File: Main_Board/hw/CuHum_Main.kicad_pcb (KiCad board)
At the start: 2 copper layers, 50 parts, among them J1 Barrel_Jack_Switch_Pin3Ring, J101 Conn_01x07, J102 Conn_01x07, J103 Conn_01x07, J104 Conn_01x07, J105 Conn_01x07, J106 Conn_01x07, J107 Conn_01x07, J108 Conn_01x07, J109 Conn_01x07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

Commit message: (WIP) Main board layout & routing
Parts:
- J101, J102, J103, J104, J105, J106, J107, J108, J109, J110, J111, J112, J113, J114, J115: footprint Connector_PinHeader_2.54mm:PinHeader_1x07_P2.54mm_Vertical -> CuHum_Main_footprints:Unit_1x07_P2.54
- moved J103 103.3 mm to (159.8, 157.2), turned to 38.571 degrees
- moved J104 92.8 mm to (178.0, 119.5), turned to 90 degrees
- moved J102 90.9 mm to (119.2, 166.6), turned to -12.857 degrees
- moved J109 79.0 mm to (138.8, 158.6), turned to 12.8573 degrees
- moved J1 75.5 mm to (145.6, 118.3), turned to 180 degrees
- moved J110 70.4 mm to (166.0, 136.8), turned to 64.2853 degrees
- moved J108 68.3 mm to (104.9, 150.9), turned to -38.5707 degrees
- moved J115 67.2 mm to (100.1, 134.0), turned to 115.714 degrees
- moved C1 65.4 mm to (139.8, 125.7), turned to -90 degrees
- moved J105 62.6 mm to (159.9, 81.8), turned to 141.428 degrees
- moved J114 61.4 mm to (89.9, 119.5), turned to -90 degrees
- moved U1 59.5 mm to (137.1, 124.8), turned to 0 degrees
- moved J101 58.8 mm to (87.8, 141.1), turned to -64.285 degrees
- moved R1 56.3 mm to (134.5, 128.2), turned to 90 degrees
- moved L1 53.6 mm to (134.4, 115.8), turned to 180 degrees
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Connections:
- U5 pad 10: UNIT_CAP_03 -> UNIT_CAP_02
- U5 pad 11: UNIT_CAP_04 -> UNIT_CAP_09
- U5 pad 12: UNIT_CAP_05 -> unconnected-(U5-LED0/ELE4-Pad12)
- U5 pad 13: UNIT_CAP_06 -> UNIT_CAP_03
- U5 pad 14: UNIT_CAP_07 -> unconnected-(U5-LED2/ELE6-Pad14)
- U5 pad 15: UNIT_CAP_08 -> unconnected-(U5-LED3/ELE7-Pad15)
- U5 pad 16: UNIT_CAP_09 -> UNIT_CAP_10
- U5 pad 17: UNIT_CAP_10 -> unconnected-(U5-LED5/ELE9-Pad17)
- U5 pad 18: UNIT_CAP_11 -> UNIT_CAP_04
- U5 pad 19: UNIT_CAP_12 -> UNIT_CAP_11
- U5 pad 8: UNIT_CAP_01 -> UNIT_CAP_15
- U5 pad 9: UNIT_CAP_02 -> UNIT_CAP_08
- U6 pad 10: UNIT_CAP_15 -> UNIT_CAP_12
- U6 pad 13: unconnected-(U6-LED1/ELE5-Pad13) -> UNIT_CAP_06
- U6 pad 15: unconnected-(U6-LED3/ELE7-Pad15) -> UNIT_CAP_13
- U6 pad 17: unconnected-(U6-LED5/ELE9-Pad17) -> UNIT_CAP_07
- U6 pad 18: unconnected-(U6-LED6/ELE10-Pad18) -> UNIT_CAP_14
- U6 pad 19: unconnected-(U6-LED7/ELE11-Pad19) -> UNIT_CAP_01
- U6 pad 8: UNIT_CAP_13 -> unconnected-(U6-ELE0-Pad8)
- U6 pad 9: UNIT_CAP_14 -> UNIT_CAP_05
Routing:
- net SPI2_MOSI: track 0.00 -> 368.9 mm, vias 0 -> 13
- net SPI2_SCK: track 0.00 -> 356.1 mm, vias 0 -> 13
- net VDD: track 8.27 -> 85.3 mm, vias 4 -> 6
- net I2C1_SDA: track 0.00 -> 70.1 mm, vias 0 -> 3
- net I2C1_SCL: track 0.00 -> 67.7 mm, vias 0 -> 2
- net UNIT_CAP_01: track 0.00 -> 59.7 mm
- net UNIT_CAP_04: track 0.00 -> 53.3 mm
- net UNIT_CAP_11: track 0.00 -> 51.8 mm
- net UNIT_CAP_14: track 0.00 -> 44.1 mm
- net UNIT_CAP_07: track 0.00 -> 41.3 mm
- net UNIT_CAP_05: track 0.00 -> 39.5 mm
- net GND: track 11.4 -> 43.0 mm, vias 25 -> 46
- net UNIT_CAP_10: track 0.00 -> 31.5 mm
- net UNIT_CAP_03: track 0.00 -> 31.4 mm
- net UNIT_CAP_08: track 0.00 -> 30.7 mm
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- added copper zone on B.Cu, net GND
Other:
- board outline added: 100 x 100 mm

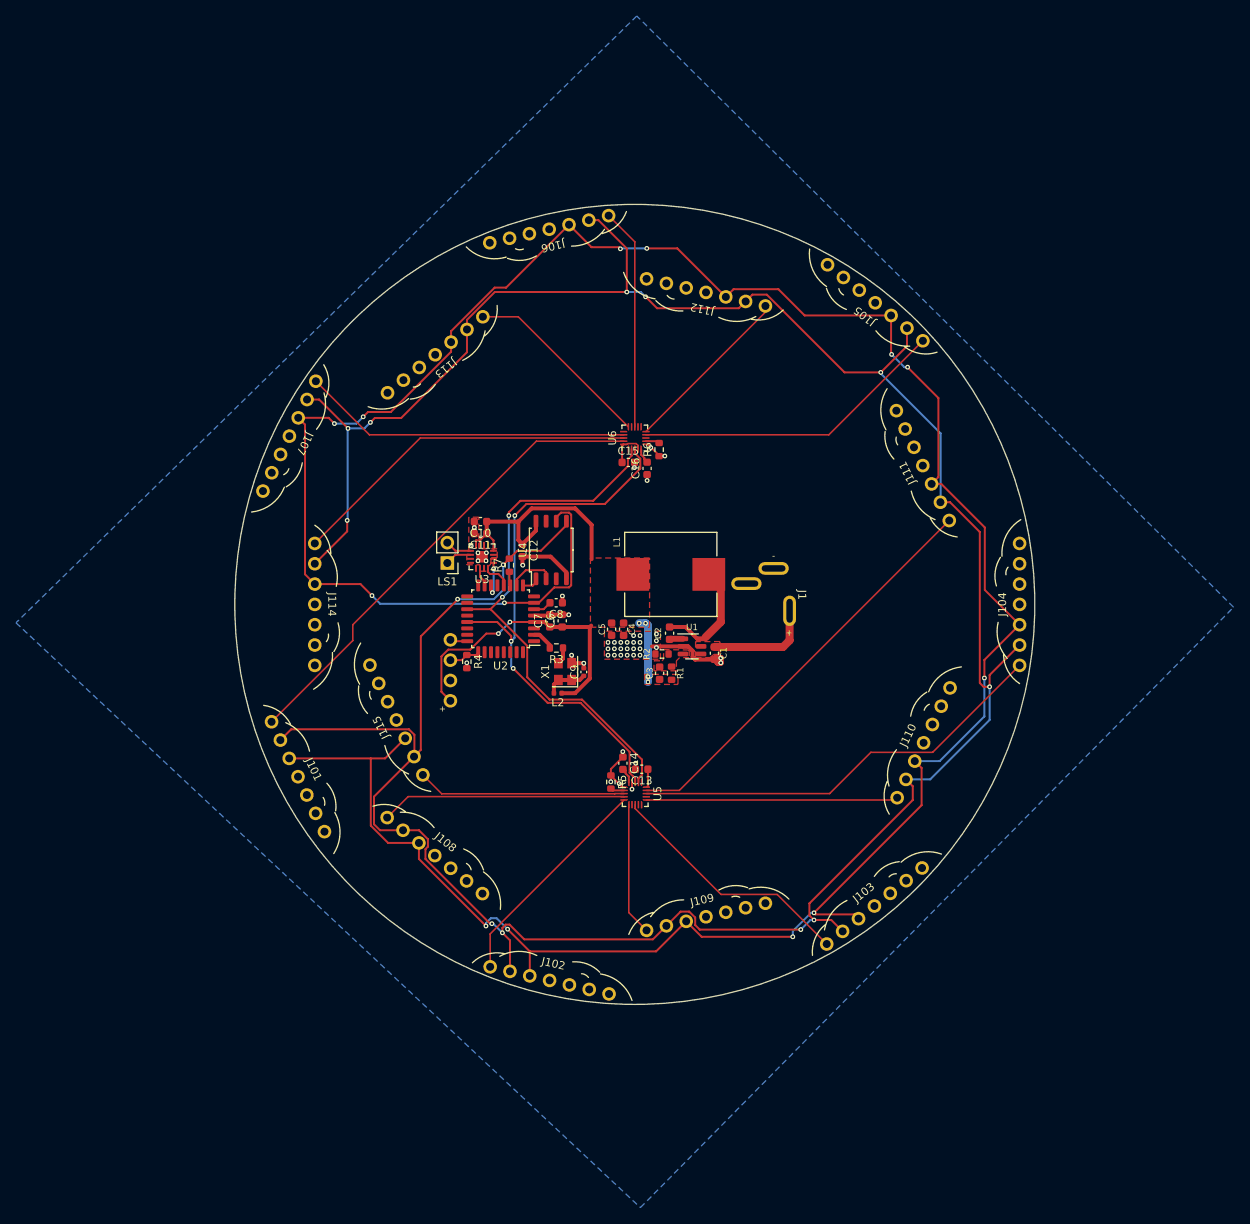
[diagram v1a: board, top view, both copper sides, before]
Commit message: Finish main board routing
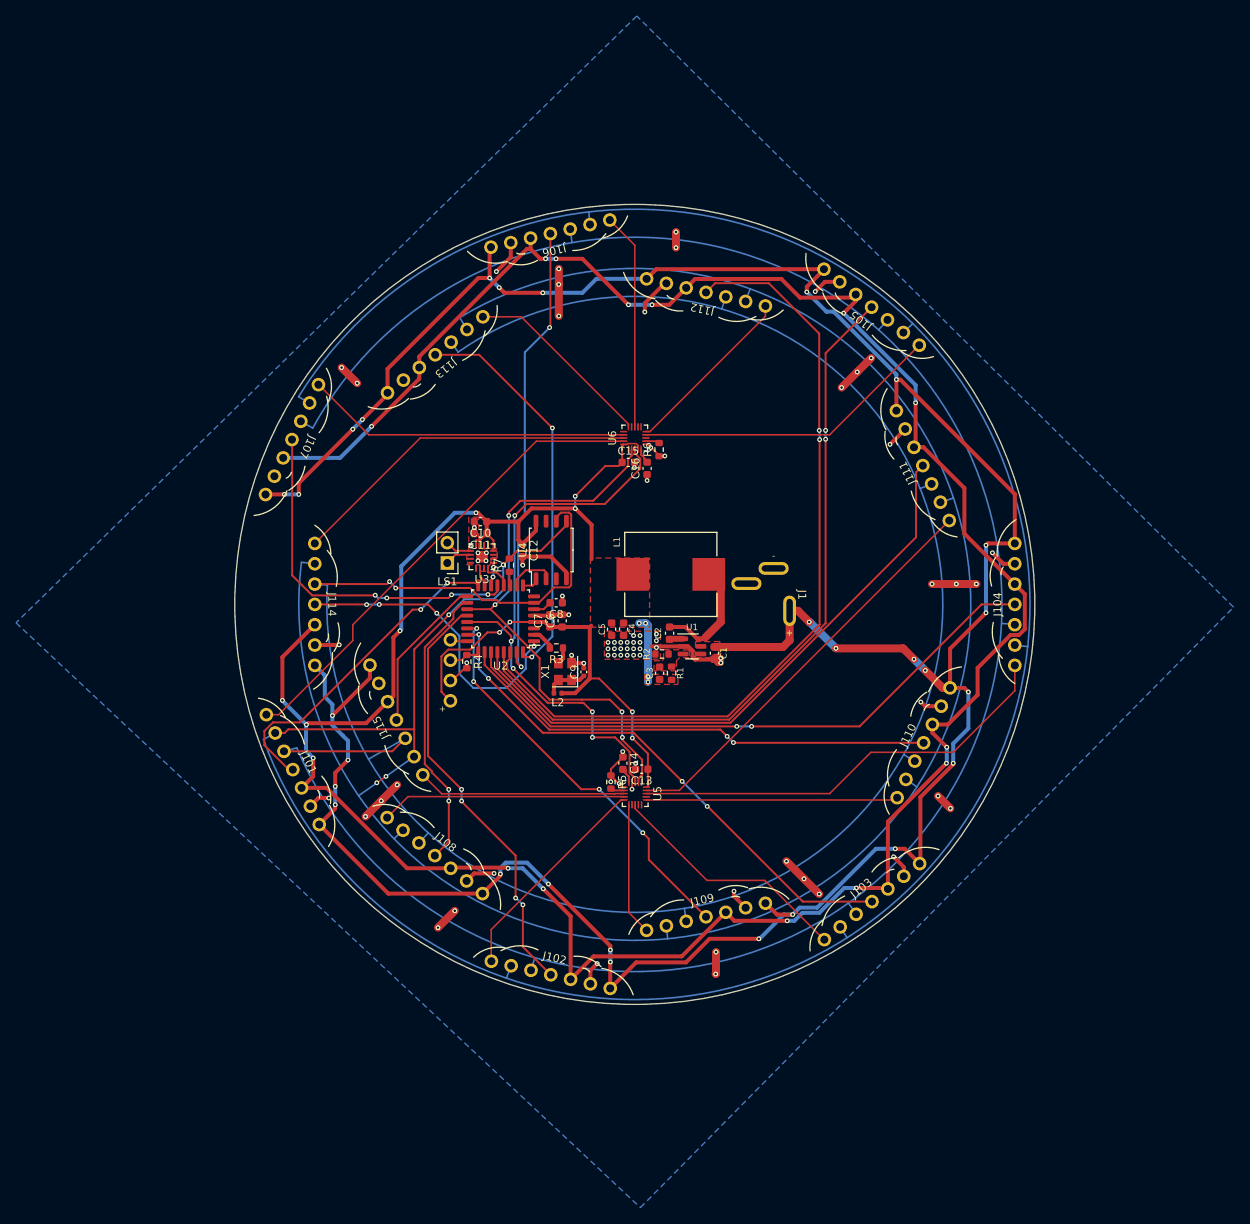
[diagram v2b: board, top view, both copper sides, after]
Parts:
- moved J101 1.10 mm to (87.2, 140.2)
- moved J102 0.72 mm to (119.4, 165.8)
- moved J105 0.71 mm to (159.5, 82.4)
- moved J103 0.63 mm to (159.6, 156.7)
- moved J104 0.60 mm to (177.4, 119.5)
- moved J106 0.57 mm to (119.3, 73.2)
- moved J107 0.54 mm to (87.0, 99.0)
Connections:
- U2 pad 1: UNIT_CS_15 -> UNIT_CS_14
- U2 pad 13: UNIT_CS_02 -> UNIT_CS_07
- U2 pad 16: UNIT_CS_03 -> UNIT_CS_01
- U2 pad 17: UNIT_CS_04 -> UNIT_CS_15
- U2 pad 18: UNIT_CS_05 -> UNIT_CS_08
- U2 pad 20: unconnected-(U2-PC6-Pad20) -> UNIT_CS_02
- U2 pad 22: UNIT_CS_06 -> UNIT_CS_09
- U2 pad 23: UNIT_CS_07 -> UNIT_CS_03
- U2 pad 26: UNIT_CS_08 -> UNIT_CS_10
- U2 pad 27: UNIT_CS_09 -> UNIT_CS_04
- U2 pad 28: UNIT_CS_10 -> UNIT_CS_11
- U2 pad 29: UNIT_CS_11 -> UNIT_CS_05
- U2 pad 31: UNIT_CS_13 -> UNIT_CS_06
- U2 pad 32: UNIT_CS_14 -> UNIT_CS_13
- U2 pad 8: UNIT_CS_01 -> unconnected-(U2-PA1-Pad8)
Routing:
- net VDD: track 85.3 -> 456.5 mm, vias 6 -> 28
- net VBUS: track 11.9 -> 359.9 mm, vias 0 -> 28
- net UNIT_CS_12: track 0.00 -> 102.2 mm, vias 0 -> 2
- net UNIT_CS_05: track 0.00 -> 91.9 mm, vias 0 -> 2
- net GND: track 43.0 -> 126.1 mm, vias 46 -> 83
- net SPI2_MOSI: track 368.9 -> 446.1 mm, vias 13 -> 4
- net UNIT_CS_04: track 0.00 -> 76.7 mm, vias 0 -> 2
- net UNIT_CS_11: track 0.00 -> 76.1 mm
- net UNIT_CS_03: track 0.00 -> 67.0 mm, vias 0 -> 4
- net SPI2_SCK: track 356.1 -> 419.2 mm, vias 13 -> 2
- net UNIT_CS_10: track 0.00 -> 60.5 mm, vias 0 -> 2
- net UNIT_CS_06: track 0.00 -> 58.0 mm, vias 0 -> 2
- net UNIT_CS_02: track 0.00 -> 53.8 mm, vias 0 -> 4
- net UNIT_CS_09: track 0.00 -> 50.8 mm, vias 0 -> 4
- net UNIT_CS_13: track 0.00 -> 49.7 mm, vias 0 -> 2
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
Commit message: Finish main board design
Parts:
- added G***: LOGO, LOGO, F.Cu at (145.7, 139.3)
- added G***: LOGO, LOGO, F.Cu at (152.1, 138.6)
- added G***: LOGO, LOGO, F.Cu at (156.9, 138.4)
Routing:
- net GND: track 126.1 -> 128.5 mm, vias 83 -> 85
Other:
- board text added: "Humming Cumulus"
- board text added: "JLCJLCJLCJLC"
- board text added: "Main Rev. 1"
